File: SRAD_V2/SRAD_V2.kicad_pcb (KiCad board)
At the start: 4 copper layers, 76.2 x 152.4 mm, 148 parts, among them IC1 STM32F767ZIT6, IC10 NCV81071BZR2G, IC2 LSM6DSVTR, IC3 MAX-M10S, IC4 MMC5983MA, IC5 AS5F31G04SND-08LIN, IC6 MS5607-02BA, IC7 TPS563200, IC8 TMCS1108A2UQDR, IC9 NCV81071BZR2G, J1 Conn_01x04_Pin, J2 S02B-XASS-1LFSN, J3 RSP-122811-02, J4 S02B-XASS-1LFSN, J5 Conn_01x02_Pin, J6 Conn_01x04_Pin, J7 Conn_01x04_Pin, Q1 NTMFS5C673NT1G, Q2 NTMFS5C673NT1G, Q3 NTMFS5C673NT1G, Q4 NTMFS5C673NT1G, Q5 MMBT3904LT3G, SW1 SLW-913535-2A-SMT, SW2 TS18-5-15-SL-160-SMT-TR, X1 Crystal

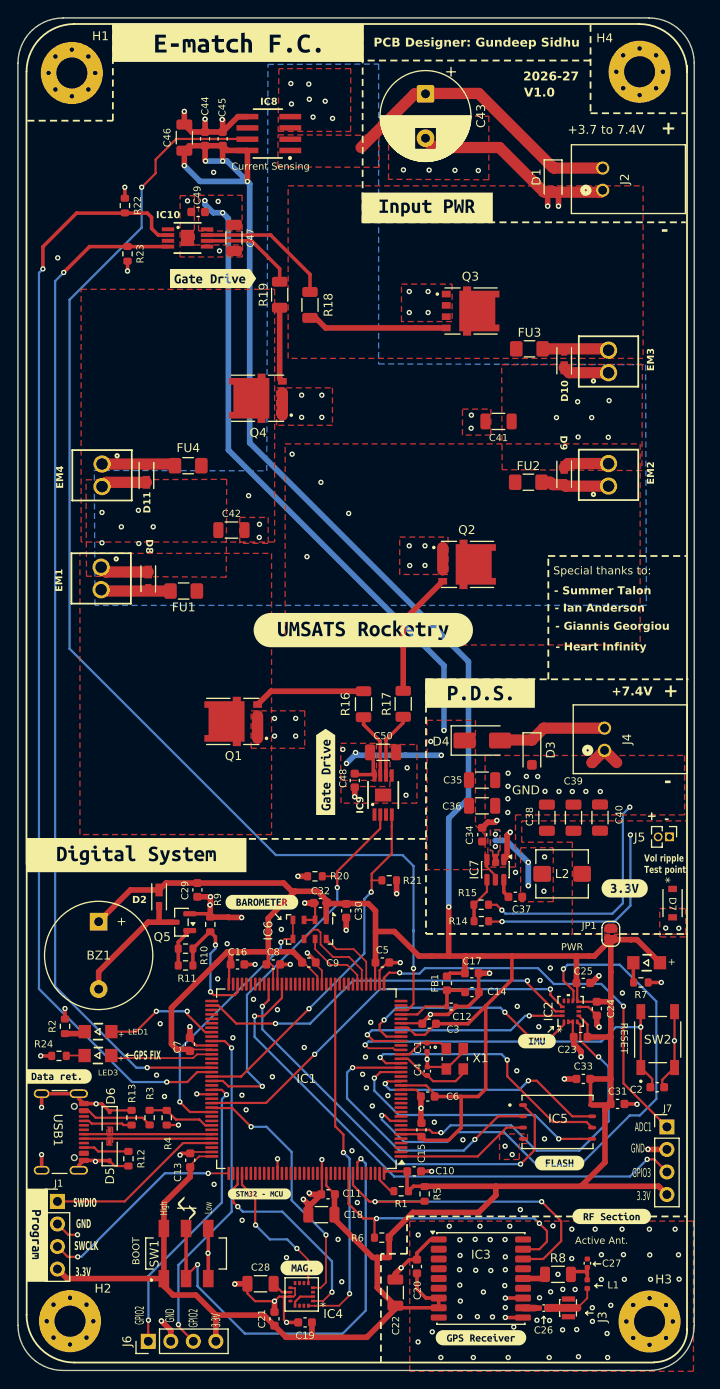
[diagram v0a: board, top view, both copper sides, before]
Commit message: In the process of adding an over discharge protection for PDS battery
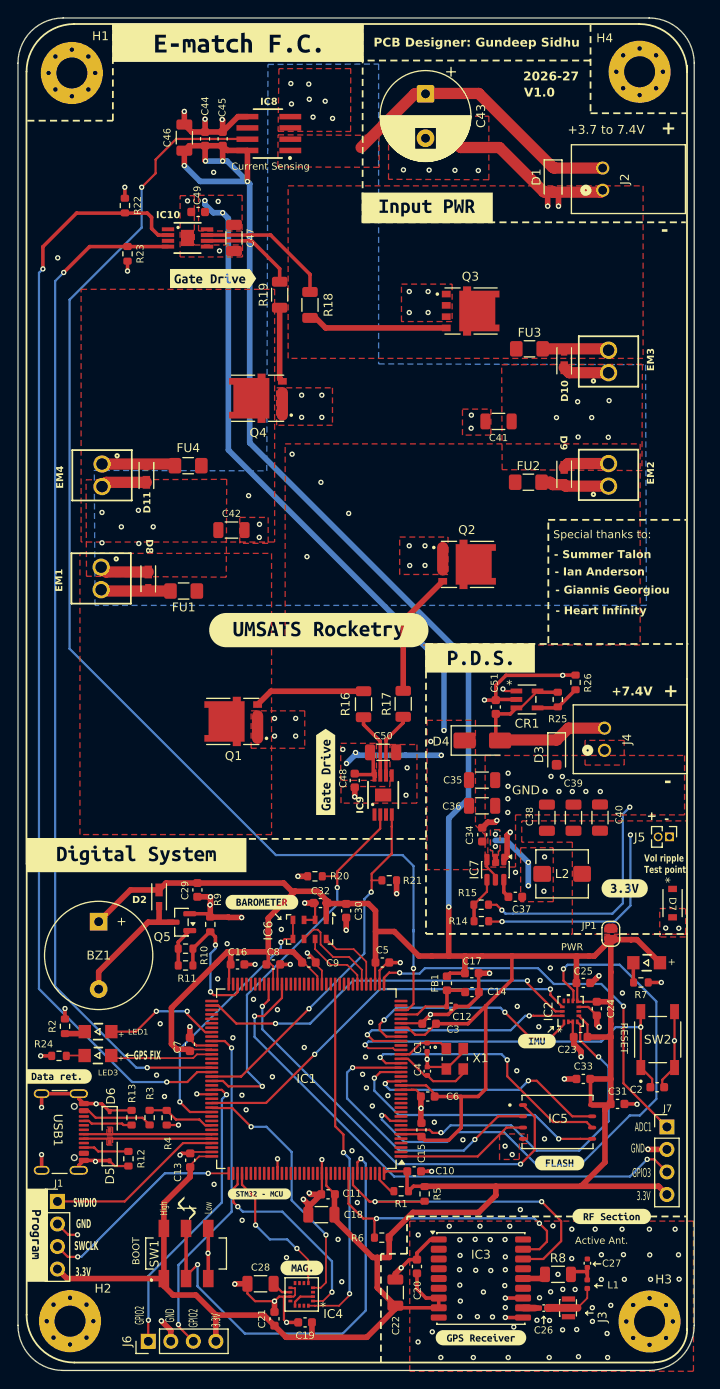
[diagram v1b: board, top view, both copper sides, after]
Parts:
- added C51: 100nF, Capacitor_SMD:C_0603_1608Metric, F.Cu at (110.1, 104.2)
- added CR1: TS941ILT, TS941ILT:SOT23-5L_STM, F.Cu at (113.6, 103.3)
- added R25: R_Small, Resistor_SMD:R_0603_1608Metric, F.Cu at (117.1, 103.4)
- added R26: 10k, Resistor_SMD:R_0603_1608Metric, F.Cu at (119.1, 101.4)
- moved kibuzzard-6A95CD47 5.01 mm to (90.2, 95.5)
- moved kibuzzard-6A9704D1 3.97 mm to (108.3, 98.7)
- moved D3 2.79 mm to (117.0, 109.3)
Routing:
- net +7.4V: track 12.4 -> 23.7 mm
- net GND: track 257.6 -> 264.0 mm, vias 217 -> 219
- net /Power Delivery System/6.6 to 7V reference: track 0.00 -> 5.12 mm
- net Enable: track 0.00 -> 1.61 mm, vias 0 -> 1

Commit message: Added component descriptions for BOM and added logos on silkscreen
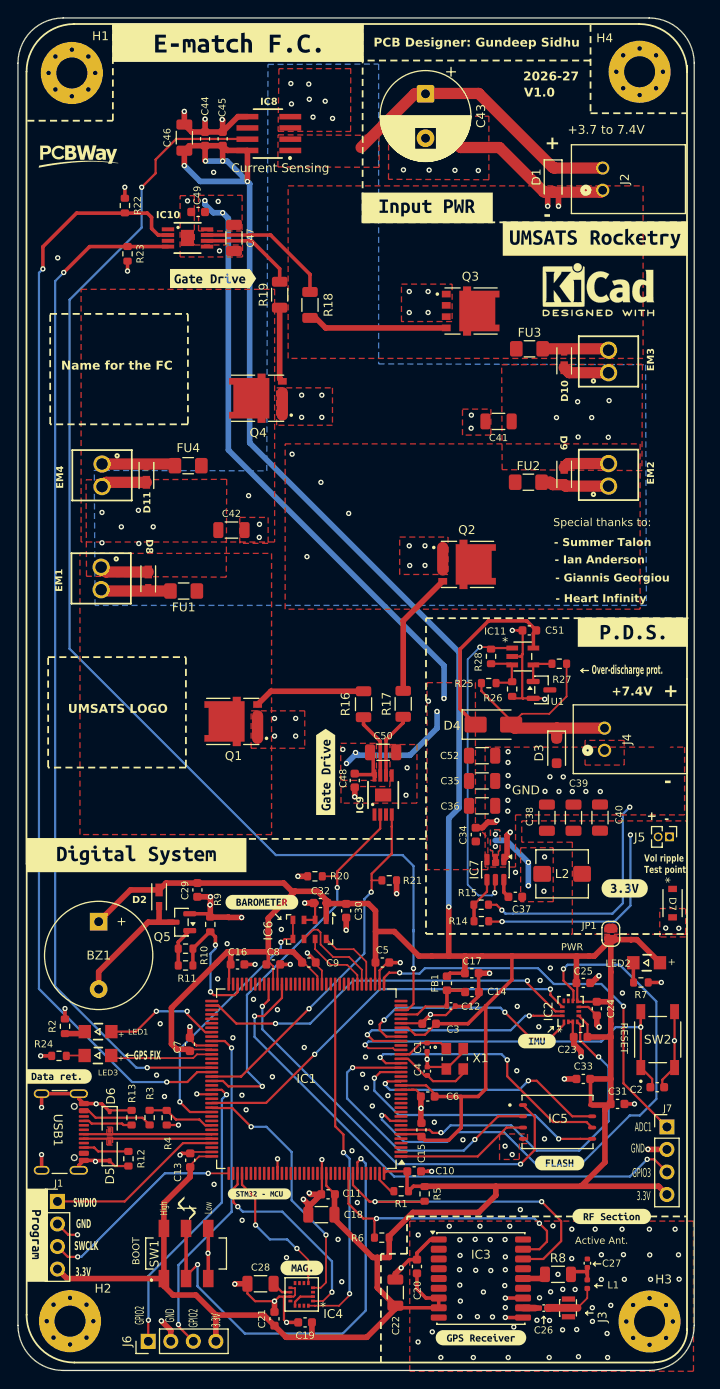
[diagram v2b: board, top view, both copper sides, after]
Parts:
- removed kibuzzard-6A95CD47: G***, kibuzzard-6A95CD47
- added C52: 10uF, Capacitor_SMD:C_1206_3216Metric, F.Cu at (108.6, 109.7)
- added G***: LOGO, pcbway:pcbway_logo, F.Cu at (63.1, 42.2)
- added R27: 20k, Resistor_SMD:R_0603_1608Metric, F.Cu at (117.3, 99.3)
- added R28: 500k, Resistor_SMD:R_0603_1608Metric, F.Cu at (109.6, 98.5)
- added REF**: KiCad-Logo2_5mm_SilkScreen, Symbol:KiCad-Logo2_5mm_SilkScreen, F.Cu at (121.7, 57.1)
- added U1: Vol Ref., Package_TO_SOT_SMD:SOT-23, F.Cu at (115.3, 102.3)
- added kibuzzard-6AA6E309: G***, kibuzzard-6AA6E309, F.Cu at (121.3, 51.4)
- C10, C11, C13, C15, C16, C2, C3, C5, C6, C7, C8, C9: value 100n -> 100nF
- C12: footprint Resistor_SMD:R_0402_1005Metric -> Capacitor_SMD:C_0402_1005Metric
- D1, D3: value SMF10CA -> TVS diode
- D10, D11, D2, D8, D9: value MSS1P5-M3/89A -> ~
- D4: value MBRA340 -> Schottky Diode
- D5, D6: value STS321050B100 -> TVS diode
- D7: value PTVS3V3S1UTR_115 -> TVS diode
- EM1, EM2, EM3, EM4: value 691210910002 -> ~
- IC1: value STM32F767ZIT6 -> ~
- IC10, IC9: value NCV81071BZR2G -> ~
- IC11: renamed from CR1; value TS941ILT -> op-amp
- IC2: value LSM6DSVTR -> ~
- IC3: value MAX-M10S -> ~
- IC4: value MMC5983MA -> ~
- IC5: value AS5F31G04SND-08LIN -> ~
- IC6: value MS5607-02BA -> ~
- IC7: value TPS563200 -> ~
- IC8: value TMCS1108A2UQDR -> ~
- J2, J4: value S02B-XASS-1LFSN -> ~
- J3: value RSP-122811-02 -> ~
- LED1, LED2, LED3: value WL-SMCW_1206 -> LED
- Q1, Q2, Q3, Q4: value NTMFS5C673NT1G -> MOSFET N-CH
- Q5: value MMBT3904LT3G -> NPN BJT
- R25: value R_Small -> 68k
- R26: value 10k -> 100k
- SW1: value SLW-913535-2A-SMT -> ~
- SW2: value TS18-5-15-SL-160-SMT-TR -> ~
- moved kibuzzard-6A9704D1 17.4 mm to (125.5, 95.8)
- moved C51 9.42 mm to (113.9, 95.6), turned to 180 degrees
- moved R25 8.00 mm to (109.3, 101.5), turned to 0 degrees
- moved R26 7.18 mm to (111.9, 102.2), turned to -90 degrees
- moved IC11 4.86 mm to (113.1, 98.5)
- moved D4 2.18 mm to (109.8, 106.2)
- moved C34 0.73 mm to (107.8, 118.6)
- moved D3 0.19 mm to (117.0, 109.1)
- moved C35 0.09 mm to (108.6, 112.5)
- moved C12 0.07 mm to (105.1, 137.9)
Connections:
- C51 pad 1: +7.4V -> +7.4VBATT
- IC11 pad 3: +7.4V -> Net-(IC11-+IN)
- IC11 pad 4: /Power Delivery System/6.6 to 7V reference -> Net-(IC11--IN)
- IC11 pad 5: +7.4V -> +7.4VBATT
- IC7 pad 5: +7.4VBATT -> Enable
- R25 pad 2: /Power Delivery System/6.6 to 7V reference -> Net-(IC11-+IN)
- R26 pad 1: /Power Delivery System/6.6 to 7V reference -> Net-(IC11-+IN)
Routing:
- net Enable: track 1.61 -> 36.0 mm, vias 1 -> 2
- net +7.4VBATT: track 90.9 -> 109.0 mm
- net Net-(IC11-+IN): track 0.00 -> 6.24 mm
- net +7.4V: track 23.7 -> 29.2 mm
- net /Power Delivery System/6.6 to 7V reference: track 5.12 -> 0.00 mm
- net Net-(IC11--IN): track 0.00 -> 4.03 mm
- net +3.3V: track 511.6 -> 510.8 mm
- net GND: track 264.0 -> 263.8 mm, vias 219 -> 221
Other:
- board text added: "3. Impedance Controlled Traces? YES - For traces on L1 with L2 as reference: - One usb differential pair: 50ohms single ended and 90ohms differential(standard tolerances) Width - 10mils, spacing - 10mils"
- board text added: "6. Board Dimensions: 152.4mm * 76.2mm (3in * 6in)"
- board text added: "Name for the FC"
- board text added: "Over-discharge prot."
- board text added: "UMSATS LOGO"
- board text removed: "3. Impedance Controlled Traces? YES - For traces on L1 with L2 as reference: - One usb differential pair: 50ohms single ended and 90ohms differential(standard tolerances) - A coplanar waveguide with ground (GCPW) : 50ohms"
- board text removed: "6. Board Dimensions: 152.4mm * 76.2mm"

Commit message: updated mounting hole dimensions
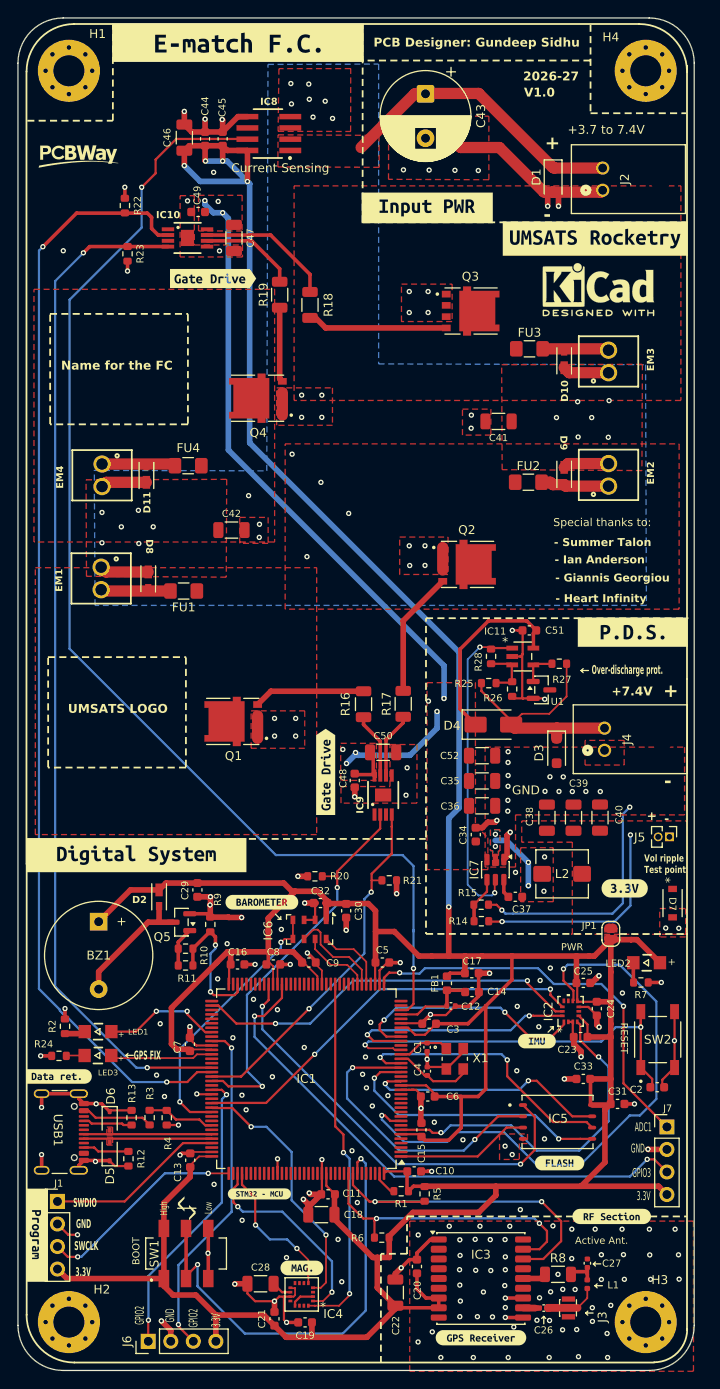
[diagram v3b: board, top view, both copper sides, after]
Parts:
- moved H4 0.70 mm to (127.0, 32.5)
- moved H3 0.44 mm to (127.0, 173.5)
- moved H1 0.41 mm to (62.0, 32.5)
- moved H2 0.16 mm to (62.0, 173.5)
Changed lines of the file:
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@@
 	(footprint "MountingHole:MountingHole_3.5mm_Pad_Via"
 		(layer "F.Cu")
-		(at 126.31 32.61)
+		(at 127 32.5)
 		(descr "Mounting Hole 3.5mm, generated by kicad-footprint-generator mountinghole.py")
 		(tags "mountinghole")
@@
 	(footprint "MountingHole:MountingHole_3.5mm_Pad_Via"
 		(layer "F.Cu")
-		(at 127.43 173.43)
+		(at 127 173.5)
 		(descr "Mounting Hole 3.5mm, generated by kicad-footprint-generator mountinghole.py")
 		(tags "mountinghole")
@@
 	(footprint "MountingHole:MountingHole_3.5mm_Pad_Via"
 		(layer "F.Cu")
-		(at 62.126155 173.396155)
+		(at 62 173.5)
 		(descr "Mounting Hole 3.5mm, generated by kicad-footprint-generator mountinghole.py")
 		(tags "mountinghole")
@@
 	(footprint "MountingHole:MountingHole_3.5mm_Pad_Via"
 		(layer "F.Cu")
-		(at 62.333845 32.746155)
+		(at 62 32.5)
 		(descr "Mounting Hole 3.5mm, generated by kicad-footprint-generator mountinghole.py")
 		(tags "mountinghole")
@@
 	(dimension
 		(type orthogonal)
+		(layer "Dwgs.User")
+		(pts
+			(xy 62 32.5) (xy 62 173.5)
+		)
+		(height -8.5)
+		(orientation 1)
+		(format
+			(prefix "")
+			(suffix "mm")
+			(units 2)
+			(units_format 0)
+			(precision 4)
+			(suppress_zeroes yes)
+		)
+		(style
+			(thickness 0.1)
+			(arrow_length 1.27)
+			(text_position_mode 0)
+			(arrow_direction outward)
+			(extension_height 0.58642)
+			(extension_offset 0.5)
+			(keep_text_aligned yes)
+		)
+		(gr_text "141mm"
+			(at 52.35 103 90)
+			(layer "Dwgs.User")
+			(effects
+				(font
+					(size 1 1)
+					(thickness 0.15)
+				)
+			)
+		)
+	)
+	(dimension
+		(type orthogonal)
+		(layer "Dwgs.User")
+		(pts
+			(xy 62 173.5) (xy 127 173.5)
+		)
+		(height 7.5)
+		(orientation 0)
+		(format
+			(prefix "")
+			(suffix "mm")
+			(units 2)
+			(units_format 0)
+			(precision 4)
+			(suppress_zeroes yes)
+		)
+		(style
+			(thickness 0.1)
+			(arrow_length 1.27)
+			(text_position_mode 0)
+			(arrow_direction outward)
+			(extension_height 0.58642)
+			(extension_offset 0.5)
+			(keep_text_aligned yes)
+		)
+		(gr_text "65mm"
+			(at 94.5 179.85 0)
+			(layer "Dwgs.User")
+			(effects
+				(font
+					(size 1 1)
+					(thickness 0.15)
+				)
+			)
+		)
+	)
+	(dimension
+		(type orthogonal)
+		(layer "Dwgs.User")
+		(pts
+			(xy 62 32.5) (xy 127 32.5)
+		)
+		(height -8)
+		(orientation 0)
+		(format
+			(prefix "")
+			(suffix "mm")
+			(units 2)
+			(units_format 0)
+			(precision 4)
+			(suppress_zeroes yes)
+		)
+		(style
+			(thickness 0.1)
+			(arrow_length 1.27)
+			(text_position_mode 0)
+			(arrow_direction outward)
+			(extension_height 0.58642)
+			(extension_offset 0.5)
+			(keep_text_aligned yes)
+		)
+		(gr_text "65mm"
+			(at 94.5 23.35 0)
+			(layer "Dwgs.User")
+			(effects
+				(font
+					(size 1 1)
+					(thickness 0.15)
+				)
+			)
+		)
+	)
+	(dimension
+		(type orthogonal)
 		(layer "F.Fab")
 		(pts
@@
 	)
 	(via
-		(at 60.739006 53.5784)
+		(at 61.3664 52.7812)
 		(size 0.6)
 		(drill 0.3)
@@
 	)
 	(segment
-		(start 61.417206 55.2284)
+		(start 63.631403 53.014203)
 		(end 64.335416 52.31019)
 		(width 0.4064)
@@
 	)
 	(via
-		(at 61.417206 55.2284)
+		(at 63.631403 53.014203)
 		(size 0.6)
 		(drill 0.3)
@@
 	)
 	(segment
-		(start 70.820005 144.828405)
-		(end 70.80841 144.84)
+		(start 70.80841 144.84)
+		(end 70.820005 144.828405)
 		(width 0.254)
 		(layer "B.Cu")
@@
 	)
 	(segment
-		(start 70.80841 144.84)
-		(end 69.600606 144.84)
+		(start 63.631403 53.014203)
+		(end 60.45 56.195606)
 		(width 0.254)
 		(layer "B.Cu")
@@
 	)
 	(segment
-		(start 69.600606 144.84)
+		(start 60.45 56.195606)
 		(end 60.45 135.689394)
 		(width 0.254)
@@
 	)
 	(segment
-		(start 60.45 135.689394)
-		(end 60.45 56.195606)
+		(start 69.600606 144.84)
+		(end 70.80841 144.84)
 		(width 0.254)
 		(layer "B.Cu")
@@
 	)
 	(segment
-		(start 60.45 56.195606)
-		(end 61.417206 55.2284)
+		(start 60.45 135.689394)
+		(end 69.600606 144.84)
 		(width 0.254)
 		(layer "B.Cu")
@@
 	)
 	(segment
-		(start 75.339006 146.4484)
-		(end 76.459001 145.328405)
-		(width 0.254)
+		(start 71.31756 50.268197)
+		(end 72.059557 51.010194)
+		(width 0.4064)
 		(layer "F.Cu")
 		(net "EM_CH3")
@@
 	)
 	(segment
+		(start 75.339006 146.4484)
+		(end 76.459001 145.328405)
+		(width 0.254)
+		(layer "F.Cu")
+		(net "EM_CH3")
+	)
+	(segment
 		(start 62.858006 48.5394)
 		(end 70.840606 48.5394)
@@
 	)
 	(segment
-		(start 71.31756 50.268197)
-		(end 72.059557 51.010194)
+		(start 72.059557 51.010194)
+		(end 73.165957 51.010194)
 		(width 0.4064)
 		(layer "F.Cu")
@@
 	)
 	(segment
-		(start 71.31756 49.016354)
-		(end 71.31756 50.268197)
-		(width 0.4064)
-		(layer "F.Cu")
-		(net "EM_CH3")
-	)
-	(segment
-		(start 59.069006 54.8284)
-		(end 59.069006 52.3284)
-		(width 0.4064)
-		(layer "F.Cu")
-		(net "EM_CH3")
-	)
-	(segment
 		(start 76.459001 145.328405)
 		(end 78.09401 145.328405)
@@
 	)
 	(segment
-		(start 72.059557 51.010194)
-		(end 73.165957 51.010194)
+		(start 71.31756 49.016354)
+		(end 71.31756 50.268197)
 		(width 0.4064)
 		(layer "F.Cu")
@@
 	)
 	(via
-		(at 59.069006 54.8284)
+		(at 59.069006 52.3284)
 		(size 0.6)
 		(drill 0.3)
@@
 	)
 	(segment
-		(start 58.625 135.944394)
-		(end 58.625 55.272406)
+		(start 69.129006 146.4484)
+		(end 73.029006 146.4484)
 		(width 0.254)
 		(layer "B.Cu")
@@
 	)
 	(segment
-		(start 58.625 55.272406)
-		(end 59.069006 54.8284)
+		(start 61.320004 138.7494)
+		(end 61.430006 138.7494)
 		(width 0.254)
 		(layer "B.Cu")
@@
 	)
 	(segment
-		(start 69.129006 146.4484)
+		(start 58.625 135.944394)
+		(end 60.9806 138.299994)
+		(width 0.254)
+		(layer "B.Cu")
+		(net "EM_CH3")
+	)
+	(segment
+		(start 58.625 52.772406)
 		(end 58.625 135.944394)
 		(width 0.254)
@@
 	)
 	(segment
-		(start 73.029006 146.4484)
+		(start 60.9806 138.409996)
+		(end 61.320004 138.7494)
+		(width 0.254)
+		(layer "B.Cu")
+		(net "EM_CH3")
+	)
+	(segment
+		(start 61.430006 138.7494)
 		(end 69.129006 146.4484)
 		(width 0.254)
@@
 	)
 	(segment
+		(start 59.069006 52.3284)
+		(end 58.625 52.772406)
+		(width 0.254)
+		(layer "B.Cu")
+		(net "EM_CH3")
+	)
+	(segment
+		(start 60.9806 138.299994)
+		(end 60.9806 138.409996)
+		(width 0.254)
+		(layer "B.Cu")
+		(net "EM_CH3")
+	)
+	(segment
 		(start 85.750406 56.2717)
 		(end 85.750409 56.271697)
@@
 		(polygon
 			(pts
-				(xy 85.180988 85.598695) (xy 63.373 85.598695) (xy 63.373 57.1246) (xy 85.180988 57.1246)
+				(xy 85.180988 85.598695) (xy 58.0644 85.598695) (xy 58.0644 57.1246) (xy 85.180988 57.1246)
 			)
 		)
@@
 		(polygon
 			(pts
-				(xy 126.368352 74.541) (xy 126.368352 93.1672) (xy 86.368352 93.1672) (xy 86.368352 74.541)
+				(xy 130.7592 74.541) (xy 130.7592 93.1672) (xy 86.368352 93.1672) (xy 86.368352 74.541)
 			)
 		)
@@
 		(polygon
 			(pts
-				(xy 126.700804 45.466695) (xy 126.700804 64.9084) (xy 86.700804 64.9084) (xy 86.700804 45.466695)
+				(xy 130.9624 45.466695) (xy 130.9624 69.6468) (xy 87.376 69.6468) (xy 87.376 45.466695)
 			)
 		)
@@
 		(polygon
 			(pts
-				(xy 63.246 86.878695) (xy 84.836004 86.878695) (xy 84.836004 118.5672) (xy 63.246 118.5672)
+				(xy 58.2168 88.4936) (xy 89.916 88.4936) (xy 89.916 118.5672) (xy 58.2168 118.5672)
 			)
 		)
